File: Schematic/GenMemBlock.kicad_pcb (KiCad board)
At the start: 4 copper layers, 99.6 x 53.3 mm, 30 parts, among them J1 MCU_HEADER, J2 ADDR_BUS, J3 DATA_BUS, J4 CART_A20, J5 CART_B10, J6 CART_B20, J7 CART_A10, U1 74HCT595, U10 74ACT16543DL, U2 74HCT595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

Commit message: working version v3
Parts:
- added J8: Conn_02x04_Odd_Even, Connector_PinHeader_2.54mm:PinHeader_2x04_P2.54mm_Vertical, F.Cu at (114.8, 104.9)
- added P1: MD-CART-FINGERS-doragasu, md-fingers:md-cart, F.Cu at (80.0, 130.8)
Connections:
- J5 pad 1: Net-(J5-Pad1) -> /H_RESET#
- J6 pad 16: GEN_RESET# -> /RESET#
- J6 pad 19: Net-(J6-Pad19) -> /S_RESET#
- J6 pad 6: /GEN_CE# -> /DO_OE
- J6 pad 9: GEN_DTACK# -> /DTACK#
- U10 pad 42: /GEN_CE# -> /DO_OE
- U8 pad 1: TX_ENABLE# -> /DO_OE
- U8 pad 28: TX_ENABLE# -> /DO_OE
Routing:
- net GND: track 471.6 -> 599.9 mm, vias 41 -> 42
- net /DO_OE: track 0.00 -> 110.2 mm, vias 0 -> 8
- net /H_RESET#: track 0.00 -> 97.0 mm, vias 0 -> 8
- net +5V: track 434.6 -> 526.3 mm, vias 35 -> 39
- net /GEN_CE#: track 61.8 -> 0.00 mm, vias 2 -> 0
- net /DTACK#: track 0.00 -> 48.0 mm, vias 0 -> 3
- net /S_RESET#: track 0.00 -> 46.2 mm, vias 0 -> 1
- net /AI_0: track 7.62 -> 45.5 mm
- net /RESET#: track 0.00 -> 37.5 mm, vias 0 -> 1
- net /AI_1: track 6.83 -> 42.1 mm
- net /AI_16: track 35.3 -> 69.5 mm
- net /AI_20: track 7.36 -> 41.1 mm, vias 0 -> 2
- net /AI_2: track 6.30 -> 38.8 mm
- net /DI_5: track 16.6 -> 47.7 mm, vias 0 -> 4
- net /AI_3: track 6.39 -> 36.6 mm, vias 0 -> 1
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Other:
- board size 99.6 x 53.3 mm -> 99.6 x 66 mm
- board text added: "!DTACK"
- board text added: "!H_RESET"
- board text added: "!RESET"
- board text added: "!S_RES"
- board text added: "!S_RESET"
- board text added: "AI_21"
- board text added: "AI_22"
- board text added: "AI_7"
- board text added: "B1"
- board text added: "B16"
- board text added: "B24"
- board text added: "B32"
- board text added: "B8"
- board text added: "DI_0"
- board text added: "DI_1"
- board text added: "DI_11"
- board text added: "DI_6"
- board text added: "DI_8"
- board text added: "digiHaze GMB v0.3 Dec 2021"
- board text removed: "digiHaze GMB v0.2 Dec 2021"

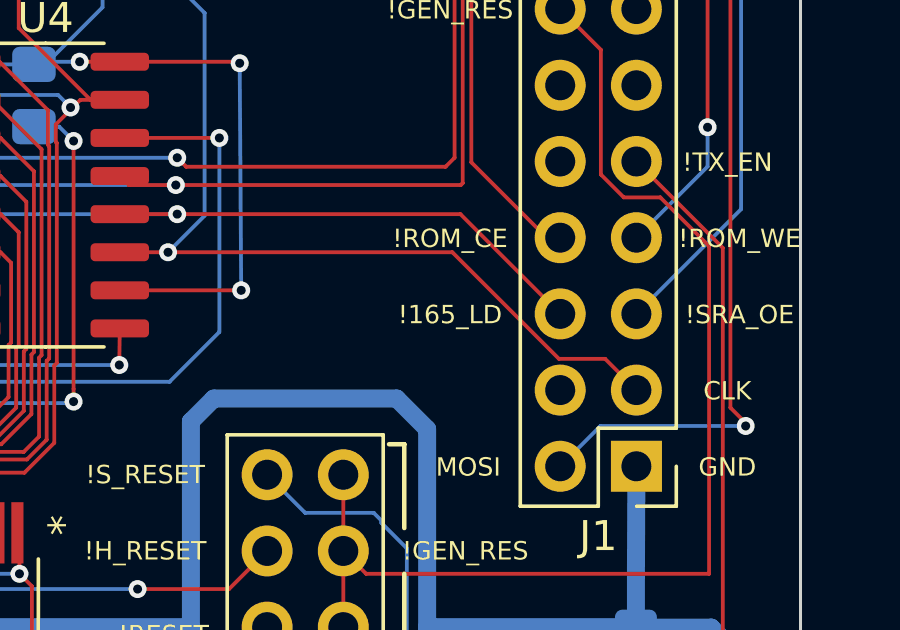
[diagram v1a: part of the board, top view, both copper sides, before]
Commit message: moved to SPI bus instead of direct control, adds SD Card
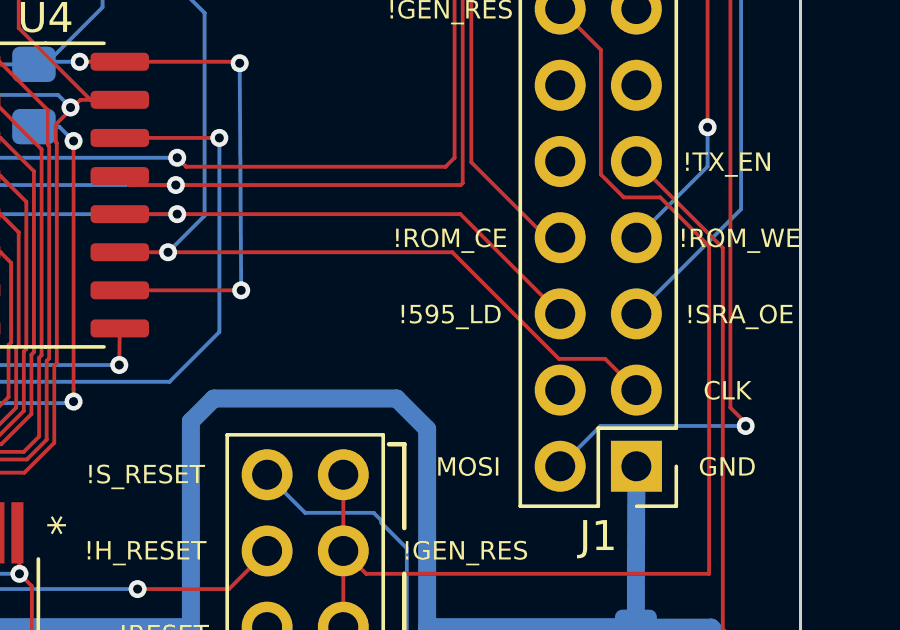
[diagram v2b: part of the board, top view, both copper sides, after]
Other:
- board text added: "!595_LD"

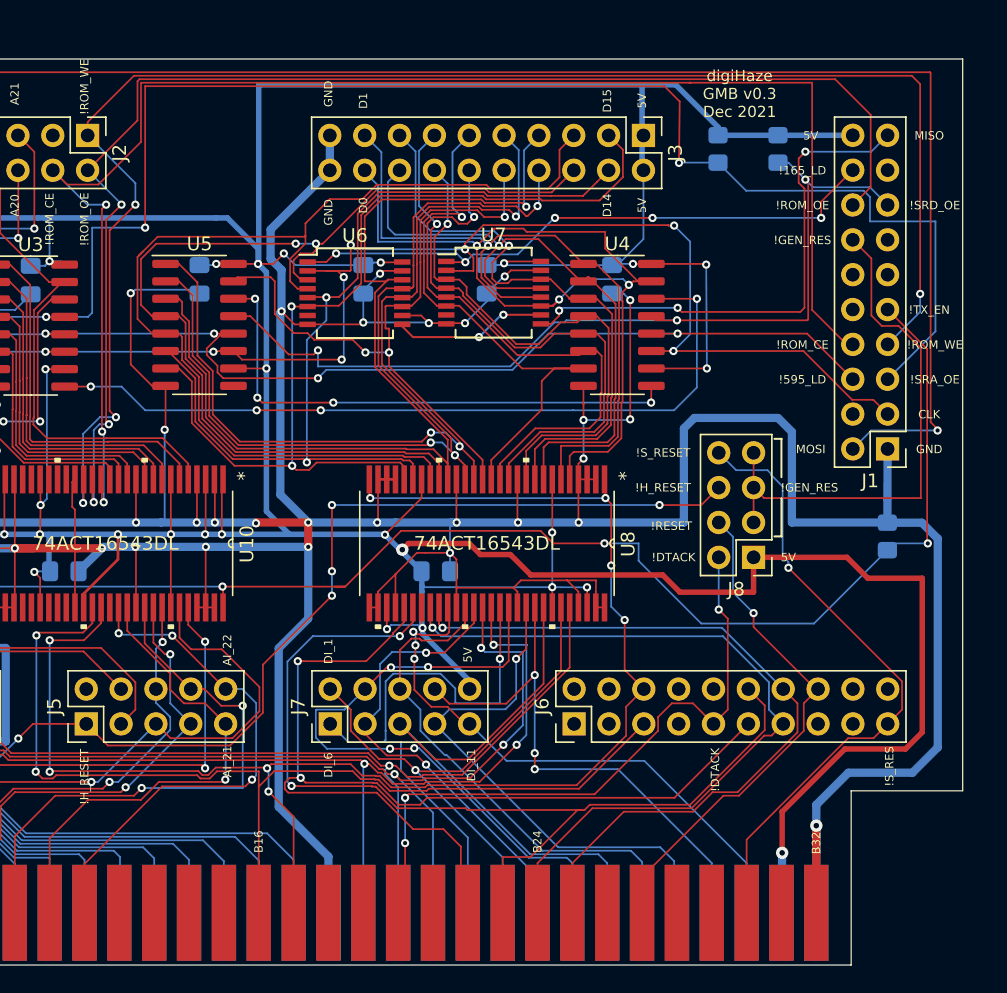
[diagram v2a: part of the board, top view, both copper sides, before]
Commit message: read/write gencart, removed reset header and use H_RESET#
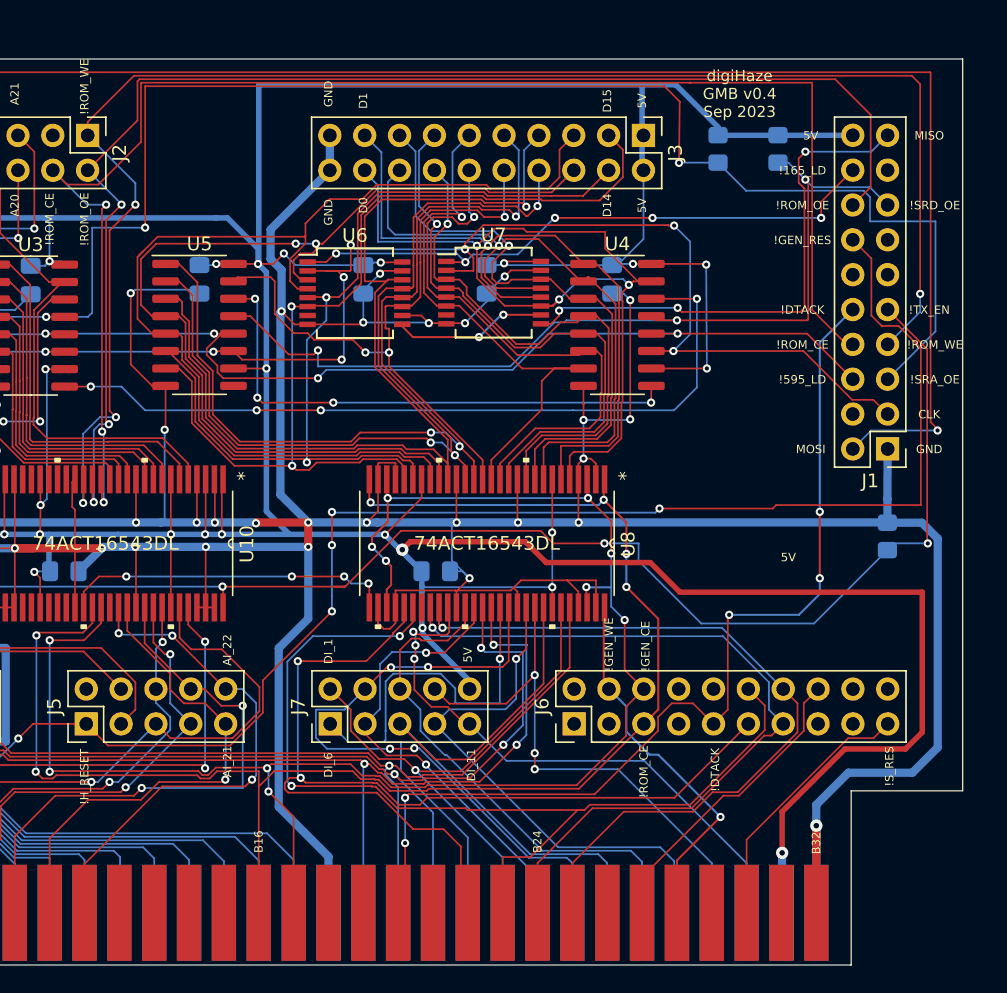
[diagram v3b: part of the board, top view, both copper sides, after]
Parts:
- removed J8: Conn_02x04_Odd_Even, Connector_PinHeader_2.54mm:PinHeader_2x04_P2.54mm_Vertical
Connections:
- J1 pad 10: Net-(J1-Pad10) -> DTACK#
- J5 pad 1: /H_RESET# -> GEN_RESET#
- J6 pad 4: Net-(J6-Pad4) -> /GEN_WE#
- J6 pad 6: /DO_OE -> /GEN_CE#
- J6 pad 9: /DTACK# -> DTACK#
- P1 pad B17: /DO_OE -> /GEN_CE#
- P1 pad B2: /H_RESET# -> GEN_RESET#
- P1 pad B20: /DTACK# -> DTACK#
- P1 pad B28: Net-(P1-PadB28) -> /GEN_WE#
- U10 pad 40: +5V -> /GEN_WE#
- U10 pad 42: /DO_OE -> /GEN_CE#
- U8 pad 1: /DO_OE -> /GEN_OE#
- U8 pad 26: GND -> /GEN_CE#
- U8 pad 28: /DO_OE -> /GEN_OE#
- U8 pad 29: GND -> /GEN_WE#
- U8 pad 3: GND -> /GEN_CE#
- U8 pad 31: +5V -> /GEN_CE#
- U8 pad 54: +5V -> /GEN_CE#
- U8 pad 56: GND -> /GEN_WE#
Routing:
- net /GEN_CE#: track 0.00 -> 120.7 mm, vias 0 -> 11
- net /DO_OE: track 110.2 -> 0.00 mm, vias 8 -> 0
- net /H_RESET#: track 97.0 -> 0.00 mm, vias 8 -> 0
- net GEN_RESET#: track 39.2 -> 133.3 mm, vias 0 -> 8
- net DTACK#: track 0.00 -> 72.7 mm, vias 0 -> 5
- net /GEN_WE#: track 0.00 -> 51.8 mm, vias 0 -> 5
- net /DTACK#: track 48.0 -> 0.00 mm, vias 3 -> 0
- net /GEN_OE#: track 73.9 -> 112.9 mm, vias 2 -> 6
- net /S_RESET#: track 46.2 -> 19.1 mm, vias 1 -> 0
- net +5V: track 526.3 -> 507.5 mm, vias 39 -> 36
- net /RESET#: track 37.5 -> 22.5 mm, vias 1 -> 0
- net GND: track 599.9 -> 588.7 mm
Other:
- board text added: "!GEN_CE"
- board text added: "!GEN_WE"
- board text added: "digiHaze GMB v0.4 Sep 2023"
- board text removed: "!RESET"
- board text removed: "!S_RESET"
- board text removed: "digiHaze GMB v0.3 Dec 2021"

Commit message: sega/microcontroller interop
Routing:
- net /GEN_WE#: track 51.8 -> 71.5 mm, vias 5 -> 6
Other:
- board text added: "digiHaze GMB v0.5 Sep 2023"
- board text removed: "digiHaze GMB v0.4 Sep 2023"

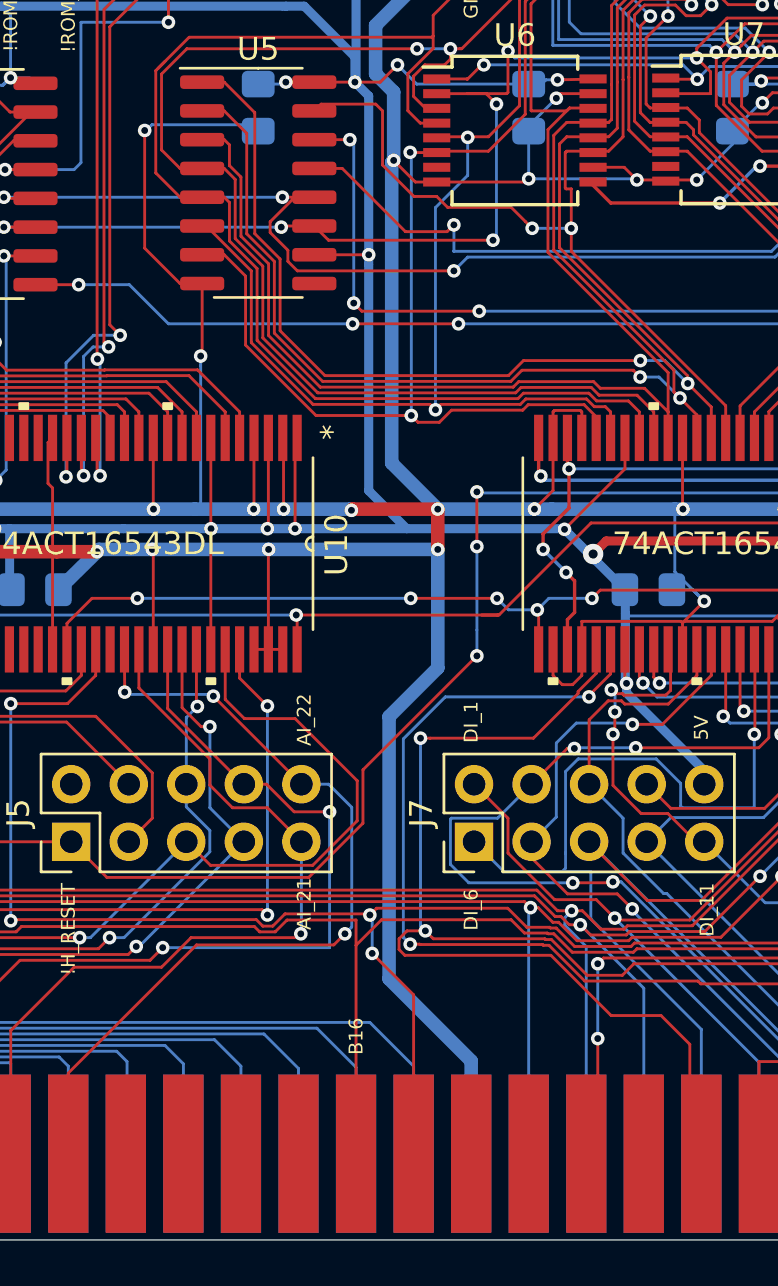
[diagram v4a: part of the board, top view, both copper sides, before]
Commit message: ROM_CE & ROM_OE on dedicated lines to allow for high-z mode
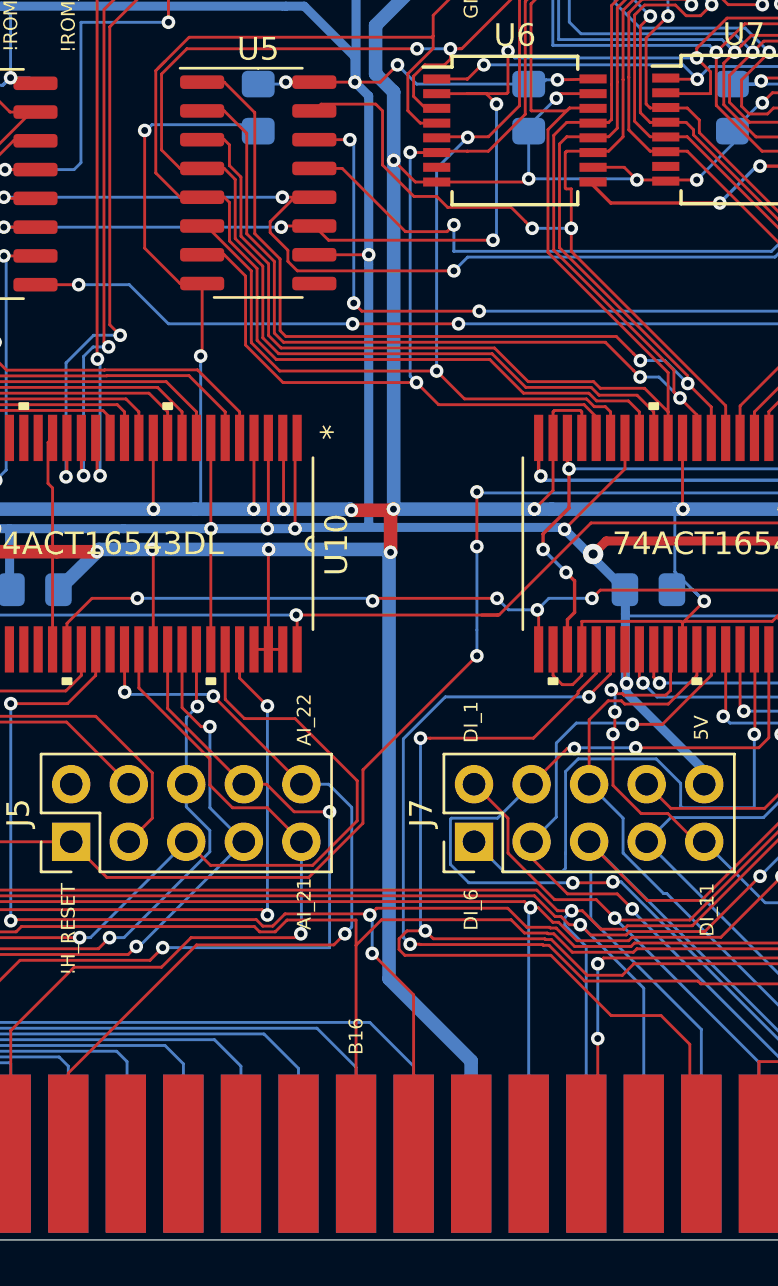
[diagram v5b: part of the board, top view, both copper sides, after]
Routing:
- net GND: track 588.7 -> 585.0 mm
- net /D14: track 66.1 -> 64.0 mm
- net /D15: track 69.6 -> 67.6 mm
- net +5V: track 507.5 -> 506.8 mm
- net /D9: track 70.7 -> 70.1 mm

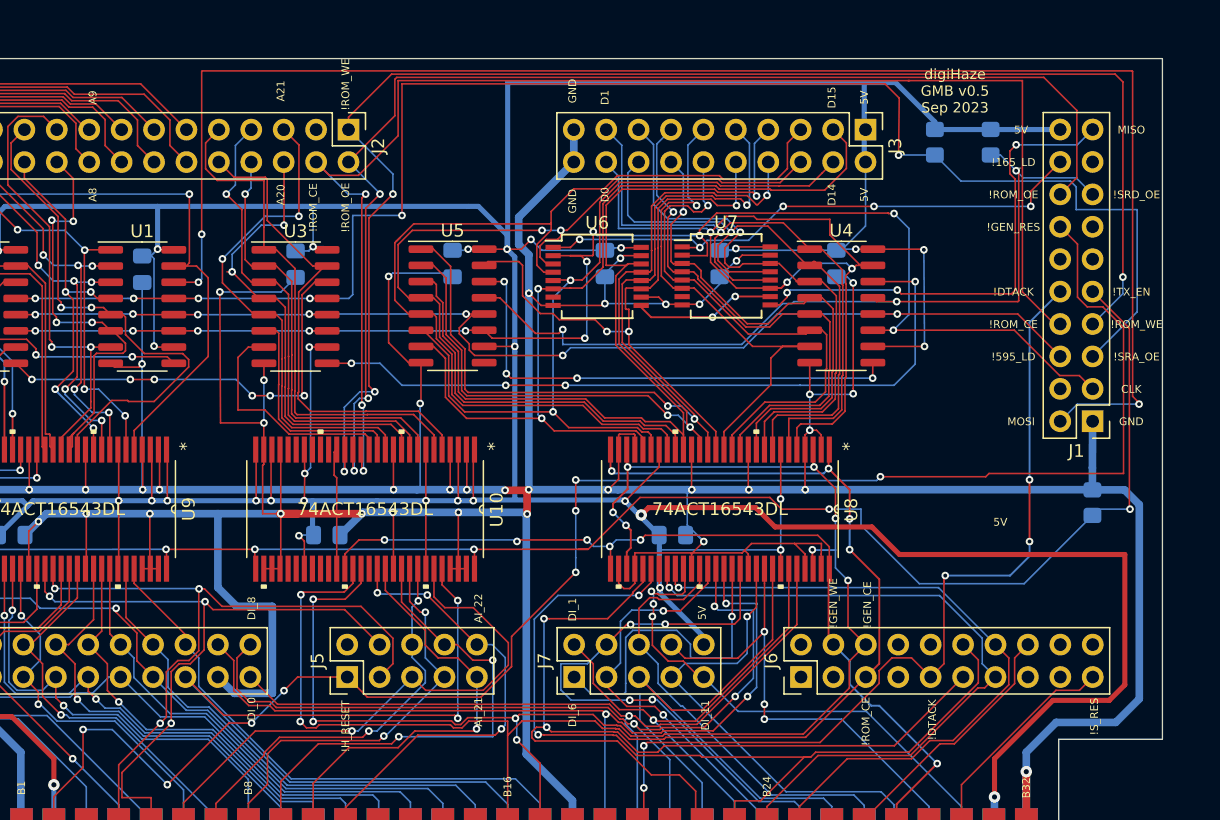
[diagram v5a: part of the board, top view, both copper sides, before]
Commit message: isolated common logic chips from mc board
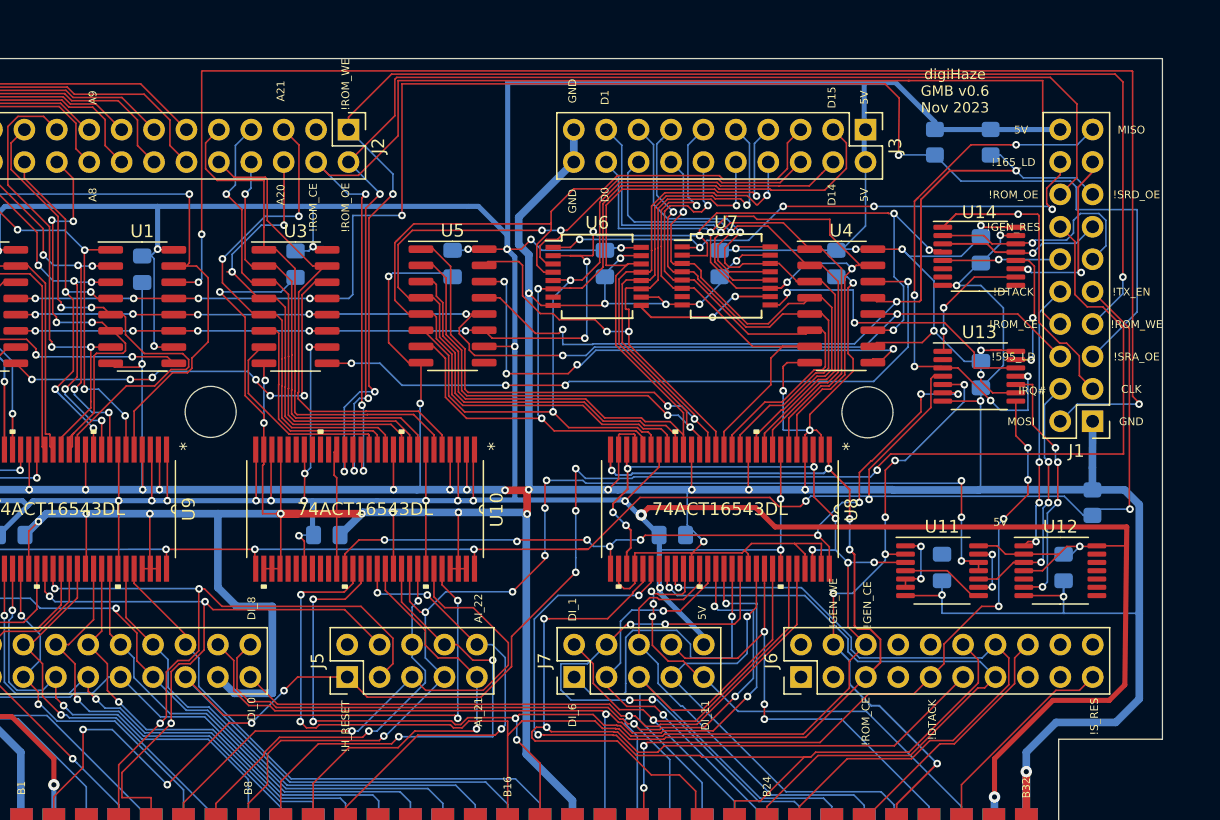
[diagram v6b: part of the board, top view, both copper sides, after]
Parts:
- added C11: 0.1pf, Capacitor_SMD:C_0805_2012Metric_Pad1.18x1.45mm_HandSolder, B.Cu at (112.8, 108.5)
- added C12: 0.1pf, Capacitor_SMD:C_0805_2012Metric_Pad1.18x1.45mm_HandSolder, B.Cu at (115.8, 93.3)
- added C13: 0.1pf, Capacitor_SMD:C_0805_2012Metric_Pad1.18x1.45mm_HandSolder, B.Cu at (122.3, 108.5)
- added C14: 0.1pf, Capacitor_SMD:C_0805_2012Metric_Pad1.18x1.45mm_HandSolder, B.Cu at (115.8, 83.6)
- added U11: 74HCT02, Package_SO:TSSOP-14_4.4x5mm_P0.65mm, F.Cu at (112.8, 108.7)
- added U12: 74HC74, Package_SO:TSSOP-14_4.4x5mm_P0.65mm, F.Cu at (122.0, 108.7)
- added U13: 74LS125, Package_SO:TSSOP-14_4.4x5mm_P0.65mm, F.Cu at (115.7, 93.5)
- added U14: 74LS139, Package_SO:TSSOP-16_4.4x5mm_P0.65mm, F.Cu at (115.7, 84.1)
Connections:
- J1 pad 10: DTACK# -> MC_DTACK#
- J1 pad 11: Net-(J1-Pad11) -> SPI_CH_ADDR_0#
- J1 pad 12: Net-(J1-Pad12) -> SPI_CLK_FB
- J1 pad 13: Net-(J1-Pad13) -> SPI_CH_ADDR_1#
- J1 pad 17: Net-(J1-Pad17) -> SPI_MISO_FB_OE#
- J1 pad 19: /SER_MISO -> MC_MISO
- J1 pad 3: /SER_CLK -> SPI_CLK
- J1 pad 4: Net-(J1-Pad4) -> IRQ#
- J6 pad 4: /GEN_WE# -> /GEN_WEREQ#
- J6 pad 9: DTACK# -> GEN_DTACK#
- P1 pad B20: DTACK# -> GEN_DTACK#
- P1 pad B28: /GEN_WE# -> /GEN_WEREQ#
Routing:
- net DTACK#: track 72.7 -> 0.00 mm, vias 5 -> 0
- net GND: track 585.0 -> 646.6 mm, vias 42 -> 46
- net GEN_DTACK#: track 0.00 -> 59.3 mm, vias 0 -> 6
- net /AI_19: track 34.4 -> 92.7 mm, vias 2 -> 9
- net /GEN_WEREQ#: track 0.00 -> 51.1 mm, vias 0 -> 6
- net MC_MISO: track 0.00 -> 43.2 mm, vias 0 -> 5
- net +5V: track 506.8 -> 549.0 mm, vias 36 -> 40
- net SPI_CLK: track 0.00 -> 23.6 mm, vias 0 -> 1
- net MC_DTACK#: track 0.00 -> 21.5 mm, vias 0 -> 3
- net GEN_DTACK_OE#: track 0.00 -> 20.0 mm, vias 0 -> 4
- net IRQ#: track 0.00 -> 19.9 mm, vias 0 -> 3
- net SPI_CH_ADDR_0#: track 0.00 -> 18.3 mm, vias 0 -> 1
- net SPI_MISO_FB_OE#: track 0.00 -> 14.6 mm, vias 0 -> 2
- net /SER_MISO: track 38.4 -> 24.6 mm, vias 3 -> 2
- net SPI_CH_ADDR_1#: track 0.00 -> 12.9 mm, vias 0 -> 1
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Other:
- outline, holes or cut-outs redrawn
- board text added: "IRQ#"
- board text added: "digiHaze GMB v0.6 Nov 2023"
- board text removed: "digiHaze GMB v0.5 Sep 2023"
